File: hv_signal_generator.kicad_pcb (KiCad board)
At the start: 2 copper layers, 83.8 x 56.1 mm, 54 parts, among them IC1 ATMEG328PU, J2 COMM_BUS, P1 FTDI_USB, P2 ISP, P3 POWER, P4 VOUT, P5 LIGHT, P6 MAGNET, P7 CONN_01X05, P8 CONN_01X03, Q1 IRF644PBF, Q2 TIP120, SW1 RESET, U2 MAX1771, U3 MCP41050, U4 HV7802, U5 AQW216, X1 16MHz

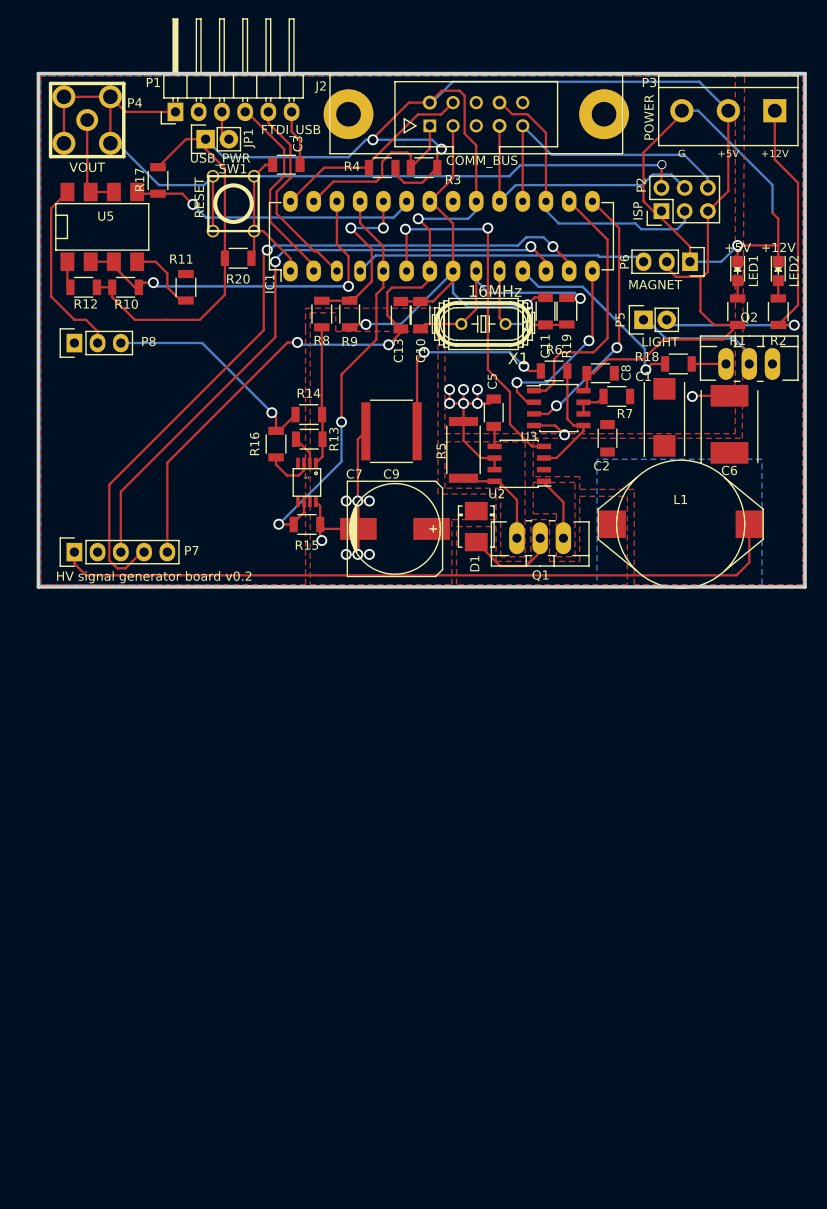
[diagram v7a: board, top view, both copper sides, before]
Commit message: Swap ATMEGA328 for Teensy
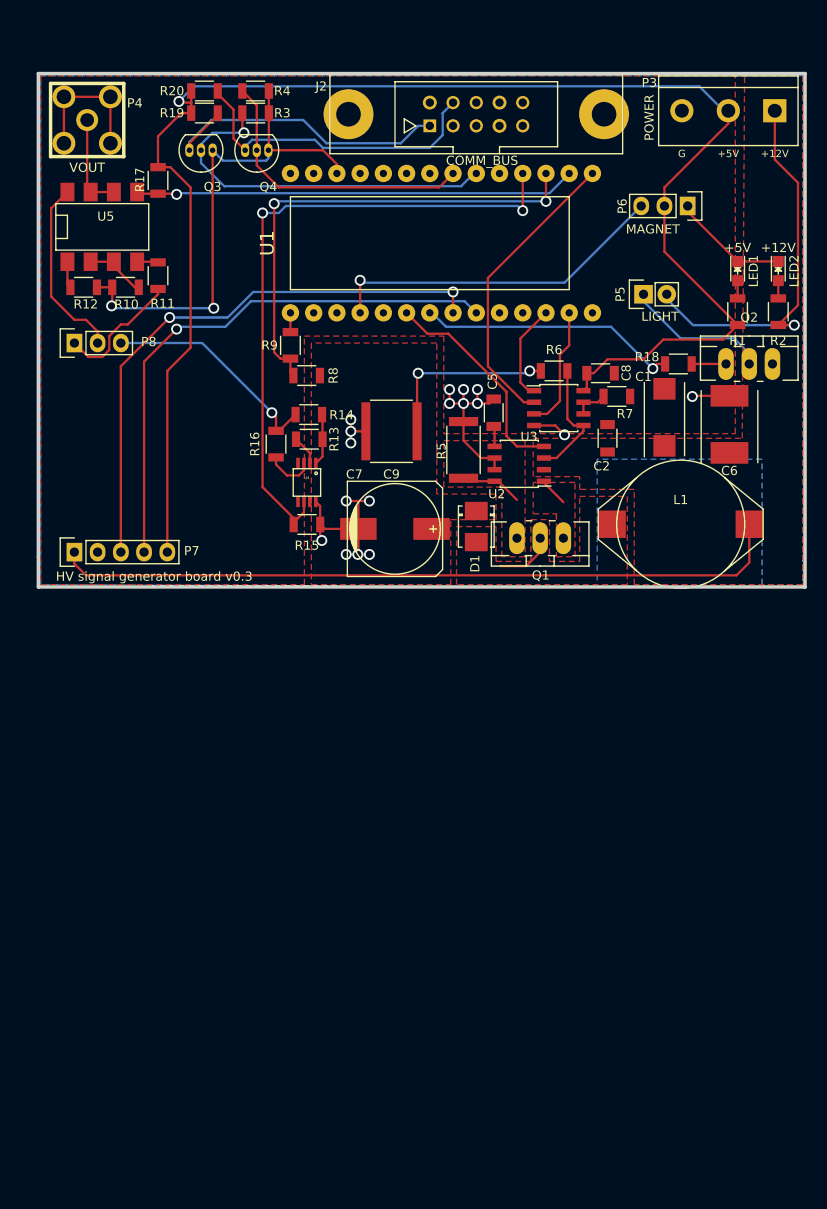
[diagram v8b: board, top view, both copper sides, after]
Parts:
- removed C10, C11: 22pF, Capacitors_SMD:C_1206
- removed C13, C3: 0.1uF, Capacitors_SMD:C_1206
- removed IC1: ATMEG328PU, Housings_DIP:DIP-28_W7.62mm_LongPads
- removed JP1: USB_PWR, Pin_Headers:Pin_Header_Straight_1x02
- removed P1: FTDI_USB, Pin_Headers:Pin_Header_Angled_1x06
- removed P2: ISP, Pin_Headers:Pin_Header_Straight_2x03
- removed SW1: RESET, footprints:SW_PUSH_6mm
- removed X1: 16MHz, footprints:SparkFun-HC49U-V
- added Q3: 2N7002, TO_SOT_Packages_THT:TO-92_Inline_Narrow_Oval, F.Cu at (35.3, 23.6)
- added Q4: 2N7002, TO_SOT_Packages_THT:TO-92_Inline_Narrow_Oval, F.Cu at (41.4, 23.6)
- added U1: Teensy_3.1, footprints:Teensy-3.1, F.Cu at (46.4, 41.4)
- R11, R12: value 374 -> 200
- R19: value 1Meg -> 5.1k
- R20: value 10k -> 5.1k
- moved R19 45.2 mm to (34.4, 19.6), turned to 0 degrees
- moved R3 19.4 mm to (40.0, 19.6)
- moved R20 18.7 mm to (34.4, 17.1), turned to 0 degrees
- moved R4 16.2 mm to (40.0, 17.1)
- moved R9 7.33 mm to (43.8, 45.0), turned to 270 degrees
- moved R8 6.93 mm to (45.6, 48.3), turned to 0 degrees
- moved P6 6.10 mm to (87.2, 29.7)
- moved R11 3.30 mm to (29.3, 37.3), turned to 90 degrees
- moved P5 2.79 mm to (82.4, 39.4)
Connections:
- net D3/A2/CURRENT_SENSE renamed A2/CURRENT_SENSE
- J2 pad 1: A4/SDA -> SDA_5V
- J2 pad 2: +5V -> Net-(J2-Pad2)
- J2 pad 4: A5/SCL -> SCL_5V
- J2 pad 7: D13/SCK -> Net-(J2-Pad7)
- J2 pad 8: D11/MOSI -> Net-(J2-Pad8)
- J2 pad 9: D12/MISO -> Net-(J2-Pad9)
- P7 pad 3: D6 -> D6/DRIVER_HI
- P7 pad 4: D7 -> D7/DRIVER_LO
- R10 pad 1: +5V -> +3.3V
- R12 pad 2: +5V -> +3.3V
- R19 pad 1: Net-(C10-Pad2) -> +5V
- R19 pad 2: Net-(C11-Pad2) -> SDA_5V
- R20 pad 1: RST -> +5V
- R20 pad 2: +5V -> SCL_5V
- R3 pad 1: +5V -> +3.3V
- R3 pad 2: A4/SDA -> SDA_3.3V
- R4 pad 1: +5V -> +3.3V
- R4 pad 2: A5/SCL -> SCL_3.3V
- U3 pad 2: D8/S_SCK -> D13/SCK
- U3 pad 3: D9/S_MOSI -> D11/MOSI
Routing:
- net GND: track 207.6 -> 98.2 mm, vias 18 -> 17
- net +5V: track 260.0 -> 170.2 mm, vias 5 -> 1
- net D7: track 81.6 -> 0.00 mm, vias 2 -> 0
- net D6: track 70.9 -> 0.00 mm, vias 2 -> 0
- net RST: track 65.9 -> 0.00 mm, vias 1 -> 0
- net D6/DRIVER_HI: track 0.00 -> 62.3 mm, vias 0 -> 2
- net D7/DRIVER_LO: track 0.00 -> 60.7 mm, vias 0 -> 1
- net +3.3V: track 0.00 -> 55.5 mm, vias 0 -> 2
- net SDA_3.3V: track 0.00 -> 41.2 mm, vias 0 -> 1
- net SDA_5V: track 0.00 -> 35.4 mm
- net SCL_5V: track 0.00 -> 35.0 mm
- net A1/HV_FB: track 19.6 -> 53.2 mm
- net A3/OUTPUT_SELECT: track 40.0 -> 6.71 mm, vias 2 -> 0
- net D12/MISO: track 32.3 -> 0.00 mm
- net SCL_3.3V: track 0.00 -> 31.9 mm
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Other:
- board text added: "HV signal generator board v0.3"
- board text removed: "HV signal generator board v0.2"
